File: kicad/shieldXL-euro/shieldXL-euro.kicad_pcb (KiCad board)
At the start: 2 copper layers, 98 x 108 mm, 132 parts, among them J101 Eurorack power, J102 IN L, J103 IN R, J104 OUT L, J105 OUT R, J106 MIDI IN, J107 MIDI OUT, J109 USB 1, J110 USB 2, J111 USB 3, J112 Pi USB, inner stack, J113 Pi USB, outer stack, J115 CORONE I/1, J116 CORONE I/2, J117 CORONE O/1, J118 CORONE O/2, J119 CORONE O/3, J120 CORONE O/4, J121 Corone, J122 ii, Q1 ASFL1-12.288MHZ-LCS-T, SW1 PVA1, SW2 PVA1, SW3 PVA1, U1 CS4270, U101 TL074, U11 TPS793475DBVR, U2 HCPL-0631-500E, X1 RASPI_BOARD_B+#_E3

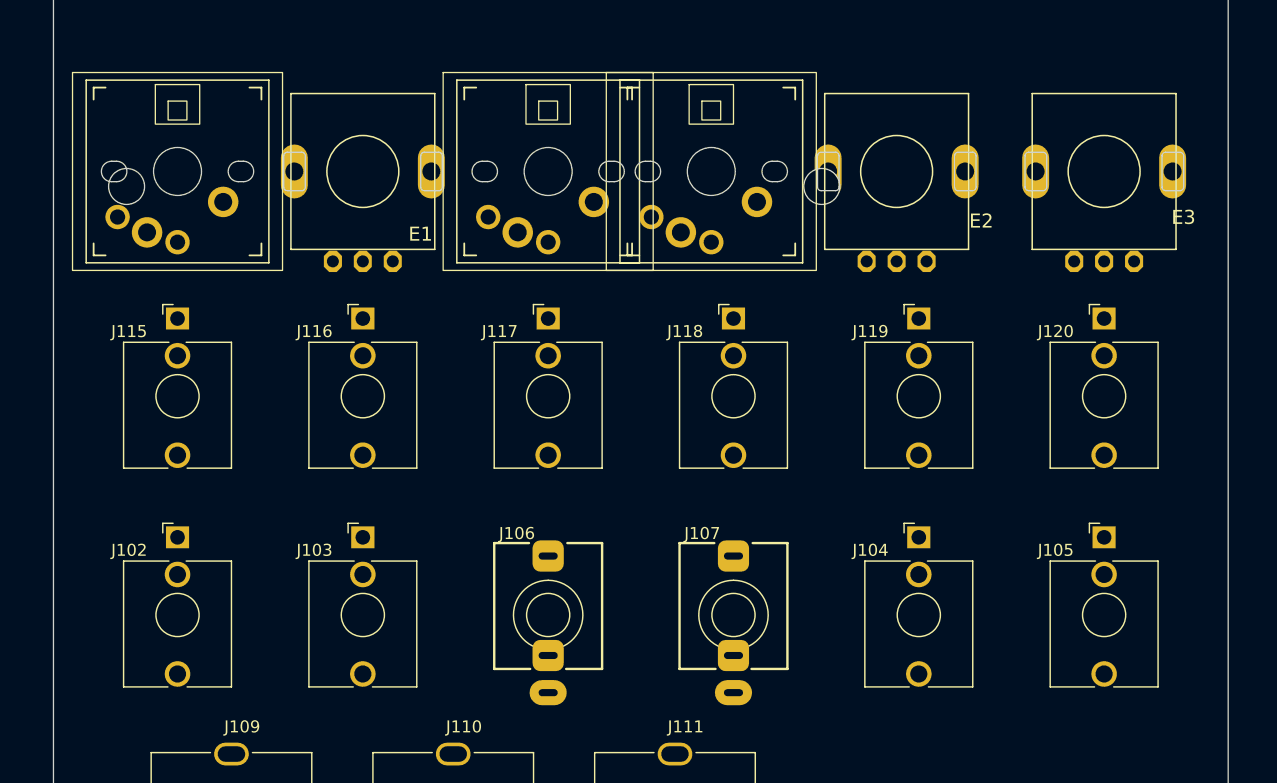
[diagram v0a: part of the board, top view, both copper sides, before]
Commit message: Board: follow the panel's fourth pass
Controls down 3 mm, crow row down 2 mm, audio and MIDI down 0.5 mm, the
CORONE outline 1 mm smaller all round; USB unchanged. Panel layers redrawn
and the panel parts re-placed.

Co-Authored-By: Claude Opus 5.5 <noreply@anthropic.com>
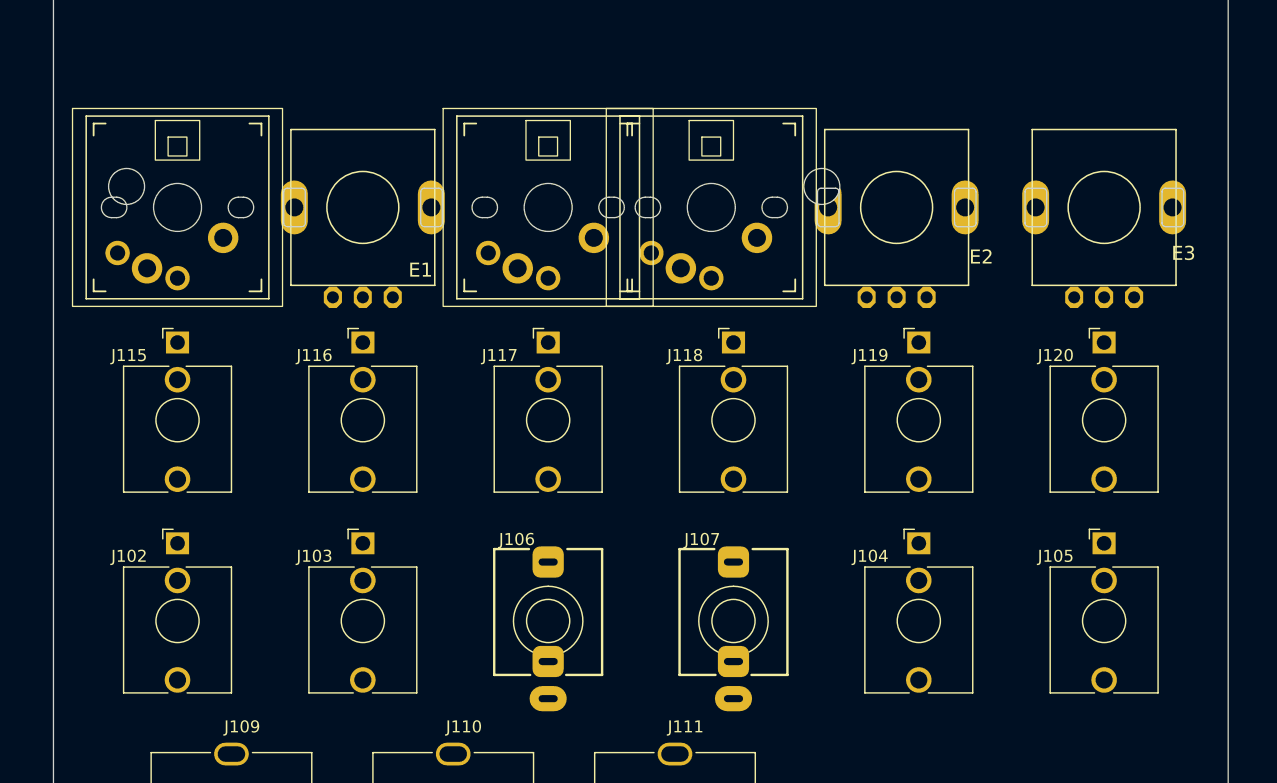
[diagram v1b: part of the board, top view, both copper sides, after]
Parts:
- moved E1 3.00 mm to (127.5, 95.0)
- moved E2 3.00 mm to (172.0, 95.0)
- moved E3 3.00 mm to (189.3, 95.0)
- moved SW1 3.00 mm to (112.0, 95.0)
- moved SW2 3.00 mm to (142.9, 95.0)
- moved SW3 3.00 mm to (156.5, 95.0)
- moved J115 2.00 mm to (112.0, 106.3)
- moved J116 2.00 mm to (127.5, 106.3)
- moved J117 2.00 mm to (142.9, 106.3)
- moved J118 2.00 mm to (158.4, 106.3)
- moved J119 2.00 mm to (173.8, 106.3)
- moved J120 2.00 mm to (189.3, 106.3)
- moved J102 0.50 mm to (112.0, 123.0)
- moved J103 0.50 mm to (127.5, 123.0)
- moved J104 0.50 mm to (173.8, 123.0)
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
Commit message: Board: K1-K3 on the D6R footprint; keys are populated
shieldXL left its keys unfitted (DNP) for builders to choose; Moirae fits
the D6R00.

Co-Authored-By: Claude Opus 5.5 <noreply@anthropic.com>
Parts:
- SW1, SW2, SW3: value PVA1 -> D6R00 F1 LFS; footprint ShieldXL:Choc_MX_combo -> MMM:SW_CK_D6R

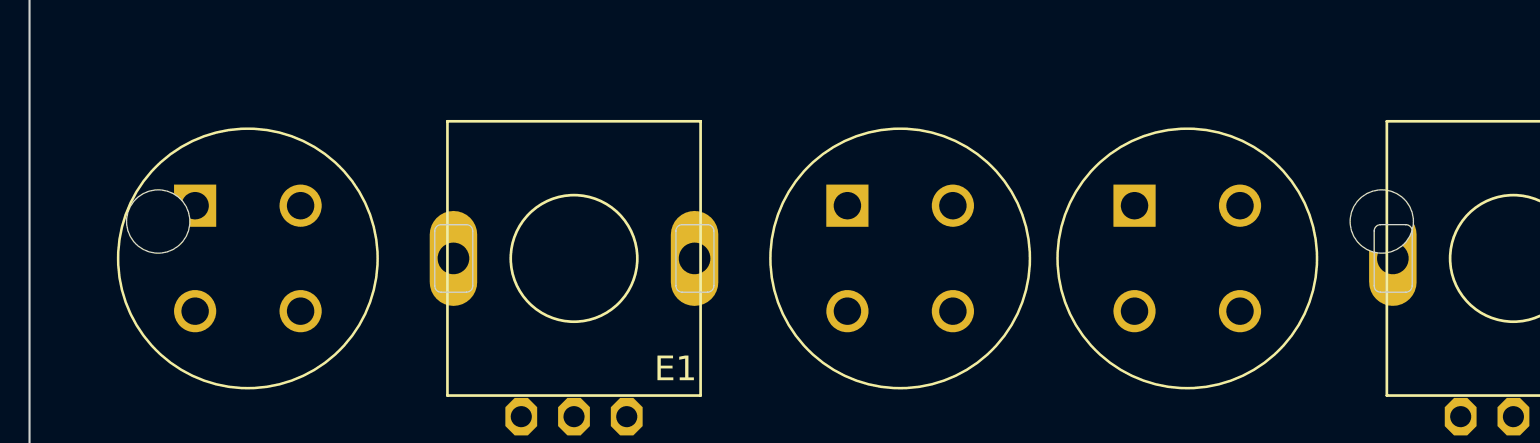
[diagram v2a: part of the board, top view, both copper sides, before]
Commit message: Pi: screw down only the two holes by the header
The other two fall on K1's and E2's pins; those corners stand on
3D-printed feet fixed to the Pi. New footprint MMM:RASPI_BOARD_B+_UPPER_HOLES
for X1, the feet drawn on User.3.

Co-Authored-By: Claude Opus 5.5 <noreply@anthropic.com>
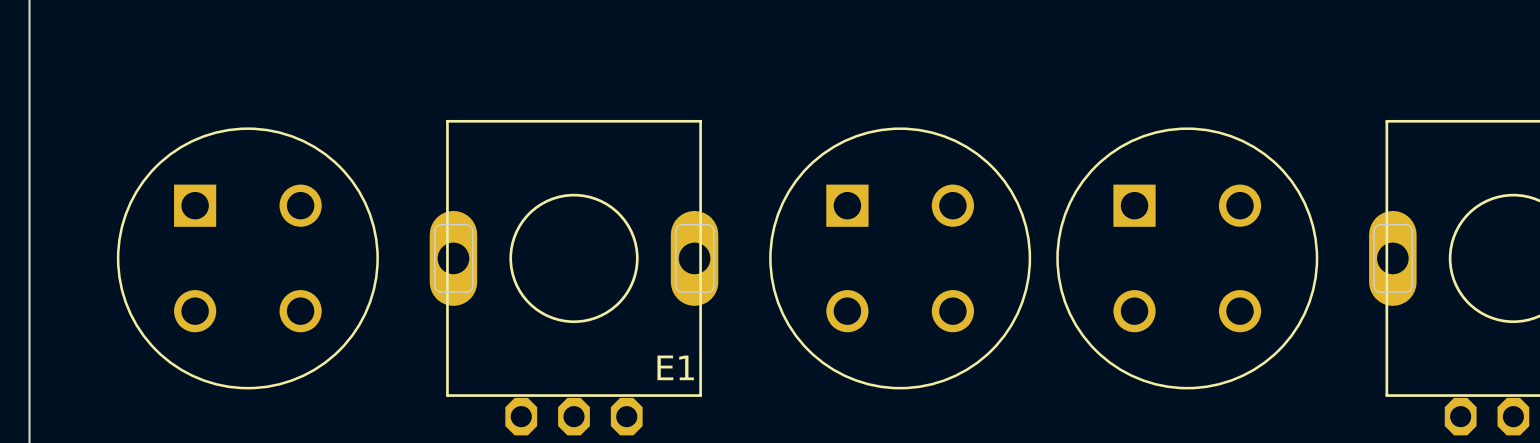
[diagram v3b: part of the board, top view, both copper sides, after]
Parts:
- X1: footprint ShieldXL:RASPI_BOARD_B+_EDGES_3DRILL -> MMM:RASPI_BOARD_B+_UPPER_HOLES
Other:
- board text added: "FOOT"

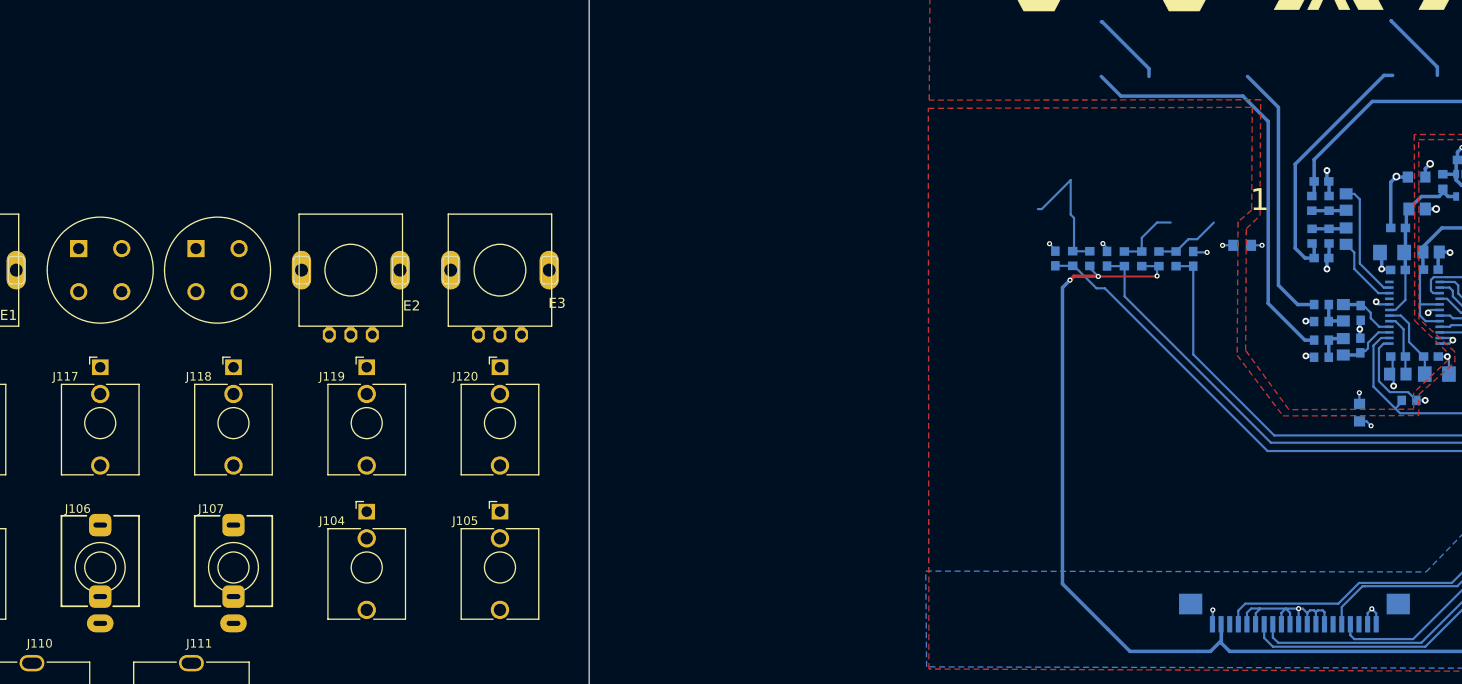
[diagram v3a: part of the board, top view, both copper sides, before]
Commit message: Board: the display's FPC slot and connector, as shieldXL had them
shieldXL's display sat with its lower-right hole on the board hole at
(319.948, 136.417), putting the module's top-left corner at (240.448,
91.417). The cable slot (26.21 x 4.06 mm, 1 mm corners) and U$1, the FPC
connector on the back, keep their offsets from that corner, now measured
from the Moirae display's corner. Slot to connector is unchanged to 0.001 mm.

Co-Authored-By: Claude Opus 5.5 <noreply@anthropic.com>
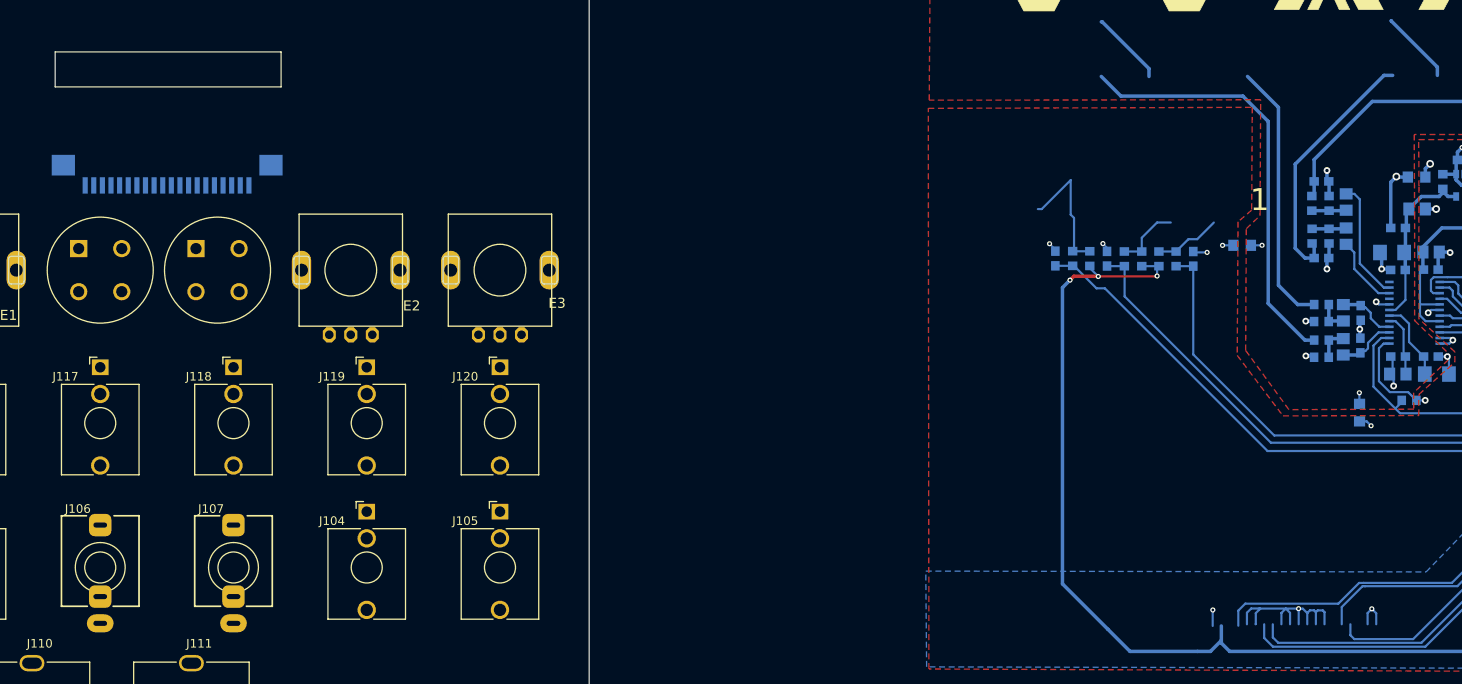
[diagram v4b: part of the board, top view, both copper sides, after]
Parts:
- moved U$1 140.4 mm to (150.2, 81.9)
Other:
- outline, holes or cut-outs redrawn
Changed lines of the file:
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@@
 	)
 	(footprint "ShieldXL:F-FPC1M20P-B310"
+		(locked yes)
 		(layer "B.Cu")
-		(at 280.9881 132.768132 90)
+		(at 150.19 81.851 90)
 		(descr "52271-2079")
 		(tags "Connector")
@@
 		(layer "Edge.Cuts")
 	)
+	(gr_rect
+		(start 137.695 69.682)
+		(end 163.903 73.741)
+		(radius 1)
+		(stroke
+			(width 0.05)
+			(type default)
+		)
+		(fill no)
+		(layer "Edge.Cuts")
+	)
 	(gr_line
 		(start 100 30)
@@
 	)
 	(segment
+		(start 333.018135 134.713295)
+		(end 336.378135 131.353295)
+		(width 0.4064)
+		(layer "F.Cu")
+		(net "Net-(SW2-PIN-1)")
+	)
+	(segment
+		(start 336.378135 131.353295)
+		(end 336.828135 131.353295)
+		(width 0.4064)
+		(layer "F.Cu")
+		(net "Net-(SW2-PIN-1)")
+	)
+	(segment
+		(start 340.666959 127.805404)
+		(end 340.673244 127.811689)
+		(width 0.254)
+		(layer "B.Cu")
+		(net "Net-(SW2-PIN-1)")
+	)
+	(segment
+		(start 340.673244 129.692428)
+		(end 340.673244 127.811689)
+		(width 0.254)
+		(layer "B.Cu")
+		(net "Net-(SW2-PIN-1)")
+	)
+	(segment
+		(start 339.012377 131.353295)
+		(end 340.673244 129.692428)
+		(width 0.254)
+		(layer "B.Cu")
+		(net "Net-(SW2-PIN-1)")
+	)
+	(segment
+		(start 336.828135 131.353295)
+		(end 339.012377 131.353295)
+		(width 0.254)
+		(layer "B.Cu")
+		(net "Net-(SW2-PIN-1)")
+	)
+	(segment
+		(start 340.666959 125.806766)
+		(end 340.666959 127.805404)
+		(width 0.254)
+		(layer "B.Cu")
+		(net "Net-(SW2-PIN-1)")
+	)
+	(segment
 		(start 324.02086 81.885983)
 		(end 324.02086 119.95747)
@@
 	)
 	(segment
-		(start 333.018135 134.713295)
-		(end 336.378135 131.353295)
-		(width 0.4064)
-		(layer "F.Cu")
-		(net "Net-(SW2-PIN-1)")
-	)
-	(segment
-		(start 336.378135 131.353295)
-		(end 336.828135 131.353295)
-		(width 0.4064)
-		(layer "F.Cu")
-		(net "Net-(SW2-PIN-1)")
-	)
-	(segment
-		(start 340.666959 127.805404)
-		(end 340.673244 127.811689)
-		(width 0.254)
-		(layer "B.Cu")
-		(net "Net-(SW2-PIN-1)")
-	)
-	(segment
-		(start 340.673244 129.692428)
-		(end 340.673244 127.811689)
-		(width 0.254)
-		(layer "B.Cu")
-		(net "Net-(SW2-PIN-1)")
-	)
-	(segment
-		(start 339.012377 131.353295)
-		(end 340.673244 129.692428)
-		(width 0.254)
-		(layer "B.Cu")
-		(net "Net-(SW2-PIN-1)")
-	)
-	(segment
-		(start 336.828135 131.353295)
-		(end 339.012377 131.353295)
-		(width 0.254)
-		(layer "B.Cu")
-		(net "Net-(SW2-PIN-1)")
-	)
-	(segment
-		(start 340.666959 125.806766)
-		(end 340.666959 127.805404)
-		(width 0.254)
-		(layer "B.Cu")
-		(net "Net-(SW2-PIN-1)")
-	)
-	(segment
-		(start 359.967718 131.335933)
-		(end 360.417718 131.335933)
-		(width 0.4064)
-		(layer "F.Cu")
-		(net "Net-(SW3-PIN-1)")
-	)
-	(segment
-		(start 356.607718 134.695933)
-		(end 359.967718 131.335933)
-		(width 0.4064)
-		(layer "F.Cu")
-		(net "Net-(SW3-PIN-1)")
-	)
-	(segment
-		(start 353.096333 130.499979)
-		(end 350.183179 130.499979)
-		(width 0.254)
-		(layer "B.Cu")
-		(net "Net-(SW3-PIN-1)")
-	)
-	(segment
-		(start 350.183179 130.499979)
-		(end 348.683412 129.000212)
-		(width 0.254)
-		(layer "B.Cu")
-		(net "Net-(SW3-PIN-1)")
-	)
-	(segment
-		(start 348.68752 125.855705)
-		(end 348.68752 127.857862)
-		(width 0.254)
-		(layer "B.Cu")
-		(net "Net-(SW3-PIN-1)")
-	)
-	(segment
-		(start 360.417718 131.335933)
-		(end 353.932287 131.335933)
-		(width 0.254)
-		(layer "B.Cu")
-		(net "Net-(SW3-PIN-1)")
-	)
-	(segment
-		(start 348.68752 127.857862)
-		(end 348.683412 127.86197)
-		(width 0.254)
-		(layer "B.Cu")
-		(net "Net-(SW3-PIN-1)")
-	)
-	(segment
-		(start 353.932287 131.335933)
-		(end 353.096333 130.499979)
-		(width 0.254)
-		(layer "B.Cu")
-		(net "Net-(SW3-PIN-1)")
-	)
-	(segment
-		(start 348.683412 129.000212)
-		(end 348.683412 127.86197)
-		(width 0.254)
-		(layer "B.Cu")
-		(net "Net-(SW3-PIN-1)")
-	)
-	(segment
 		(start 343.702762 131.490283)
 		(end 342.746937 131.490283)
@@
 	)
 	(segment
+		(start 359.967718 131.335933)
+		(end 360.417718 131.335933)
+		(width 0.4064)
+		(layer "F.Cu")
+		(net "Net-(SW3-PIN-1)")
+	)
+	(segment
+		(start 356.607718 134.695933)
+		(end 359.967718 131.335933)
+		(width 0.4064)
+		(layer "F.Cu")
+		(net "Net-(SW3-PIN-1)")
+	)
+	(segment
+		(start 353.096333 130.499979)
+		(end 350.183179 130.499979)
+		(width 0.254)
+		(layer "B.Cu")
+		(net "Net-(SW3-PIN-1)")
+	)
+	(segment
+		(start 350.183179 130.499979)
+		(end 348.683412 129.000212)
+		(width 0.254)
+		(layer "B.Cu")
+		(net "Net-(SW3-PIN-1)")
+	)
+	(segment
+		(start 348.68752 125.855705)
+		(end 348.68752 127.857862)
+		(width 0.254)
+		(layer "B.Cu")
+		(net "Net-(SW3-PIN-1)")
+	)
+	(segment
+		(start 360.417718 131.335933)
+		(end 353.932287 131.335933)
+		(width 0.254)
+		(layer "B.Cu")
+		(net "Net-(SW3-PIN-1)")
+	)
+	(segment
+		(start 348.68752 127.857862)
+		(end 348.683412 127.86197)
+		(width 0.254)
+		(layer "B.Cu")
+		(net "Net-(SW3-PIN-1)")
+	)
+	(segment
+		(start 353.932287 131.335933)
+		(end 353.096333 130.499979)
+		(width 0.254)
+		(layer "B.Cu")
+		(net "Net-(SW3-PIN-1)")
+	)
+	(segment
+		(start 348.683412 129.000212)
+		(end 348.683412 127.86197)
+		(width 0.254)
+		(layer "B.Cu")
+		(net "Net-(SW3-PIN-1)")
+	)
+	(segment

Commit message: Board: first layout pass; USB-C on the left of the USB row
All parts brought onto the board and placed by hand. J108 stands at 90 deg
at the left end of the USB row (nudged 0.75 mm left to clear the panel's
I/L label), J109-J111 moved right to make room; the panel follows. The
placement script keeps J108 turned. Copper pours refilled.

Known DRC: AGND track across J112 pin 9/10 and -12V_IN across J101 pins
5/6 (shorts), R103/R104 courtyards overlap.

Co-Authored-By: Claude Opus 5.5 <noreply@anthropic.com>
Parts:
- added J108: USB-C 5V, MMM:USB_C_Receptacle_Molex_2047110001_Vertical, F.Cu at (107.0, 142.0)
- C113, D103, F101, J101, J112, J113, J121, J122, R101, R102, R103, R104, R105, R106, R107, R108, R110, R111, R112, U101: moved to B.Cu
- moved R18 185.1 mm to (180.1, 65.1), turned to -90 degrees
- moved R16 182.0 mm to (176.1, 54.9)
- moved C18 182.0 mm to (172.2, 54.9)
- moved R5 182.0 mm to (167.6, 58.2)
- moved R6 182.0 mm to (179.5, 54.9)
- moved U2 182.0 mm to (176.2, 59.3)
- moved C15 168.8 mm to (118.7, 53.4)
- moved C17 168.8 mm to (118.7, 62.3)
- moved R10 168.8 mm to (118.7, 73.8)
- moved R7 168.8 mm to (118.7, 67.7)
- moved R8 168.8 mm to (118.7, 69.6)
- moved R9 168.8 mm to (118.7, 71.8)
- moved U11 168.8 mm to (135.3, 53.8)
- moved C1 168.8 mm to (131.4, 63.6)
- moved C11 168.8 mm to (123.3, 68.6)
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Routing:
- net AGND: track 32.3 -> 197.4 mm, vias 12 -> 2
- net -12V: track 0.00 -> 142.2 mm, vias 0 -> 3
- net /eurorack/OUTR_AMP: track 0.00 -> 129.4 mm, vias 0 -> 3
- net +12V: track 0.00 -> 117.4 mm, vias 0 -> 3
- net +3V3: track 334.9 -> 220.6 mm, vias 10 -> 12
- net /eurorack/OUTL_AMP: track 0.00 -> 106.7 mm, vias 0 -> 2
- net /eurorack/II_SCL: track 0.00 -> 100.5 mm
- net /eurorack/+12V_IN: track 0.00 -> 92.9 mm
- net /eurorack/II_SDA: track 0.00 -> 90.6 mm
- net /eurorack/MIDI_OUT_R: track 0.00 -> 89.3 mm, vias 0 -> 1
- net (no net): track 87.2 -> 0.55 mm
- net /eurorack/CRW_OUT4: track 0.00 -> 85.1 mm
- net /eurorack/OUTR_FB: track 0.00 -> 81.3 mm, vias 0 -> 4
- net /eurorack/MIDI_OUT_T: track 0.00 -> 75.0 mm, vias 0 -> 2
- net /eurorack/CRW_OUT3: track 0.00 -> 72.2 mm
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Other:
- outline, holes or cut-outs redrawn
